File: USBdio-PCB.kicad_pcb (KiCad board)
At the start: 2 copper layers, 82.5 x 101.6 mm, 67 parts, among them IC1 ATMEGA328-P, P0 RELAY_(JSM1A-12V-4), P1 RELAY_(JSM1A-12V-4), P2 RELAY_(JSM1A-12V-4), P3 RELAY_(JSM1A-12V-4), P4 RELAY_(JSM1A-12V-4), P5 RELAY_(JSM1A-12V-4), P6 RELAY_(JSM1A-12V-4), P7 RELAY_(JSM1A-12V-4), P8 CONN_01X03, Q1 Q_NPN_BEC, Q10 Q_NPN, Q11 Q_NPN, Q12 Q_NPN, Q13 Q_NPN, Q14 Q_NPN, Q15 Q_NPN, Q16 Q_NPN, Q17 Q_NPN, Q2 Q_NPN_BEC, Q3 Q_NPN_BEC, Q4 Q_NPN_BEC, Q5 Q_NPN_BEC, Q6 Q_NPN_BEC, Q7 Q_NPN_BEC, Q8 Q_NPN_BEC, Q9 Q_NPN_BEC, U1 NCV7805BDTRKG, X1 CRYSTAL_SMD

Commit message: almost finish with traces.
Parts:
- moved P8 82.8 mm to (117.0, 63.6), turned to 90 degrees
- moved D4 39.4 mm to (158.6, 114.7), turned to 180 degrees
- moved D3 39.4 mm to (174.5, 114.7), turned to 180 degrees
- moved R22 39.1 mm to (164.1, 118.8)
- moved P4 39.1 mm to (148.4, 112.0)
- moved Q13 39.0 mm to (160.1, 119.2)
- moved P5 39.0 mm to (164.3, 112.0)
- moved Q12 39.0 mm to (176.0, 119.2)
- moved R21 38.2 mm to (179.1, 118.7)
- moved R23 32.3 mm to (147.8, 118.5)
- moved P3 32.0 mm to (132.4, 112.0)
- moved Q14 32.0 mm to (144.1, 119.3)
- moved D5 31.5 mm to (142.6, 114.8), turned to 180 degrees
- moved R24 27.6 mm to (148.1, 96.3)
- moved P2 27.5 mm to (132.4, 89.6)
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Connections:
- CONN_1 pad A2: GND -> Net-(CONN_1-PadA2)
- CONN_1 pad A3: GND -> Net-(CONN_1-PadA2)
- CONN_1 pad B1: Net-(CONN_1-PadA1) -> RLY4
- CONN_1 pad B10: RLY5 -> Net-(CONN_1-PadA1)
- CONN_1 pad B11: RLY6 -> Net-(CONN_1-PadA2)
- CONN_1 pad B12: RLY7 -> Net-(CONN_1-PadA2)
- CONN_1 pad B2: Net-(CONN_1-PadA1) -> RLY5
- CONN_1 pad B3: GND -> RLY6
- CONN_1 pad B4: GND -> RLY7
- CONN_1 pad B9: RLY4 -> Net-(CONN_1-PadA1)
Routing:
- net Net-(D1-Pad1): track 0.00 -> 333.6 mm, vias 0 -> 4
- net Net-(CONN_1-PadA1): track 0.00 -> 243.4 mm, vias 0 -> 2
- net +5V: track 0.00 -> 185.1 mm
- net Net-(CONN_1-PadB6): track 0.00 -> 166.0 mm
- net Net-(CONN_1-PadA5): track 0.00 -> 157.6 mm
- net Net-(CONN_1-PadB5): track 0.00 -> 155.2 mm, vias 0 -> 2
- net Net-(CONN_1-PadA6): track 0.00 -> 139.8 mm
- net Net-(CONN_1-PadB7): track 0.00 -> 132.1 mm
- net Net-(CONN_1-PadA7): track 0.00 -> 123.5 mm
- net Net-(CONN_1-PadB8): track 0.00 -> 117.5 mm
- net Net-(CONN_1-PadA8): track 0.00 -> 115.2 mm
- net Net-(CONN_1-PadA4): track 0.00 -> 96.0 mm, vias 0 -> 2
- net Net-(IC1-Pad15): track 0.00 -> 94.7 mm, vias 0 -> 2
- net Net-(IC1-Pad16): track 0.00 -> 82.5 mm, vias 0 -> 2
- net Net-(IC1-Pad17): track 0.00 -> 78.4 mm, vias 0 -> 2
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- added copper zone on B.Cu, net GND

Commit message: finished traces
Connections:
- CONN_1 pad A1: Net-(CONN_1-PadA1) -> GND
- CONN_1 pad A10: RLY1 -> RLY3
- CONN_1 pad A11: RLY2 -> Net-(CONN_1-PadA11)
- CONN_1 pad A12: RLY3 -> Net-(CONN_1-PadA12)
- CONN_1 pad A2: Net-(CONN_1-PadA2) -> GND
- CONN_1 pad A3: Net-(CONN_1-PadA2) -> Net-(CONN_1-PadA3)
- CONN_1 pad A7: Net-(CONN_1-PadA7) -> RLY0
- CONN_1 pad A8: Net-(CONN_1-PadA8) -> RLY1
- CONN_1 pad A9: RLY0 -> RLY2
- CONN_1 pad B1: RLY4 -> Net-(CONN_1-PadA12)
- CONN_1 pad B10: Net-(CONN_1-PadA1) -> Net-(CONN_1-PadB10)
- CONN_1 pad B11: Net-(CONN_1-PadA2) -> GND
- CONN_1 pad B12: Net-(CONN_1-PadA2) -> GND
- CONN_1 pad B2: RLY5 -> Net-(CONN_1-PadA12)
- CONN_1 pad B3: RLY6 -> RLY4
- CONN_1 pad B4: RLY7 -> RLY5
- CONN_1 pad B5: Net-(CONN_1-PadB5) -> RLY6
- CONN_1 pad B6: Net-(CONN_1-PadB6) -> RLY7
- CONN_1 pad B9: Net-(CONN_1-PadA1) -> Net-(CONN_1-PadB9)
- D9 pad 2: Net-(CONN_1-PadA1) -> Net-(CONN_1-PadA12)
- P0 pad 1: Net-(CONN_1-PadA1) -> Net-(CONN_1-PadA12)
- P1 pad 1: Net-(CONN_1-PadA1) -> Net-(CONN_1-PadA12)
- P2 pad 1: Net-(CONN_1-PadA1) -> Net-(CONN_1-PadA12)
- P3 pad 1: Net-(CONN_1-PadA1) -> Net-(CONN_1-PadA12)
- P4 pad 1: Net-(CONN_1-PadA1) -> Net-(CONN_1-PadA12)
- P5 pad 1: Net-(CONN_1-PadA1) -> Net-(CONN_1-PadA12)
- P6 pad 1: Net-(CONN_1-PadA1) -> Net-(CONN_1-PadA12)
- P7 pad 1: Net-(CONN_1-PadA1) -> Net-(CONN_1-PadA12)
- R10 pad 2: Net-(CONN_1-PadA8) -> Net-(CONN_1-PadA6)
- R12 pad 2: Net-(CONN_1-PadB5) -> Net-(CONN_1-PadB7)
- R14 pad 2: Net-(CONN_1-PadB6) -> Net-(CONN_1-PadB8)
- R16 pad 2: Net-(CONN_1-PadB7) -> Net-(CONN_1-PadB9)
- R18 pad 2: Net-(CONN_1-PadB8) -> Net-(CONN_1-PadB10)
- R2 pad 2: Net-(CONN_1-PadA4) -> Net-(CONN_1-PadA11)
- R4 pad 2: Net-(CONN_1-PadA5) -> Net-(CONN_1-PadA3)
- R6 pad 2: Net-(CONN_1-PadA6) -> Net-(CONN_1-PadA4)
- R8 pad 2: Net-(CONN_1-PadA7) -> Net-(CONN_1-PadA5)
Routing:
- net Net-(CONN_1-PadA1): track 243.4 -> 0.00 mm, vias 2 -> 0
- net Net-(CONN_1-PadA12): track 0.00 -> 223.5 mm, vias 0 -> 2
- net Net-(CONN_1-PadB6): track 166.0 -> 0.00 mm
- net Net-(CONN_1-PadB5): track 155.2 -> 0.00 mm, vias 2 -> 0
- net Net-(CONN_1-PadA3): track 0.00 -> 139.9 mm, vias 0 -> 1
- net Net-(CONN_1-PadA7): track 123.5 -> 0.00 mm
- net Net-(CONN_1-PadB10): track 0.00 -> 115.9 mm, vias 0 -> 1
- net Net-(CONN_1-PadA8): track 115.2 -> 0.00 mm
- net Net-(CONN_1-PadB9): track 0.00 -> 111.0 mm, vias 0 -> 1
- net Net-(CONN_1-PadA11): track 0.00 -> 80.3 mm, vias 0 -> 1
- net Net-(CONN_1-PadB8): track 117.5 -> 172.3 mm, vias 0 -> 1
- net Net-(CONN_1-PadA5): track 157.6 -> 121.4 mm, vias 0 -> 1
- net Net-(CONN_1-PadA4): track 96.0 -> 128.0 mm, vias 2 -> 1
- net Net-(CONN_1-PadA6): track 139.8 -> 111.8 mm, vias 0 -> 1
- net Net-(CONN_1-PadB7): track 132.1 -> 155.2 mm, vias 0 -> 1
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
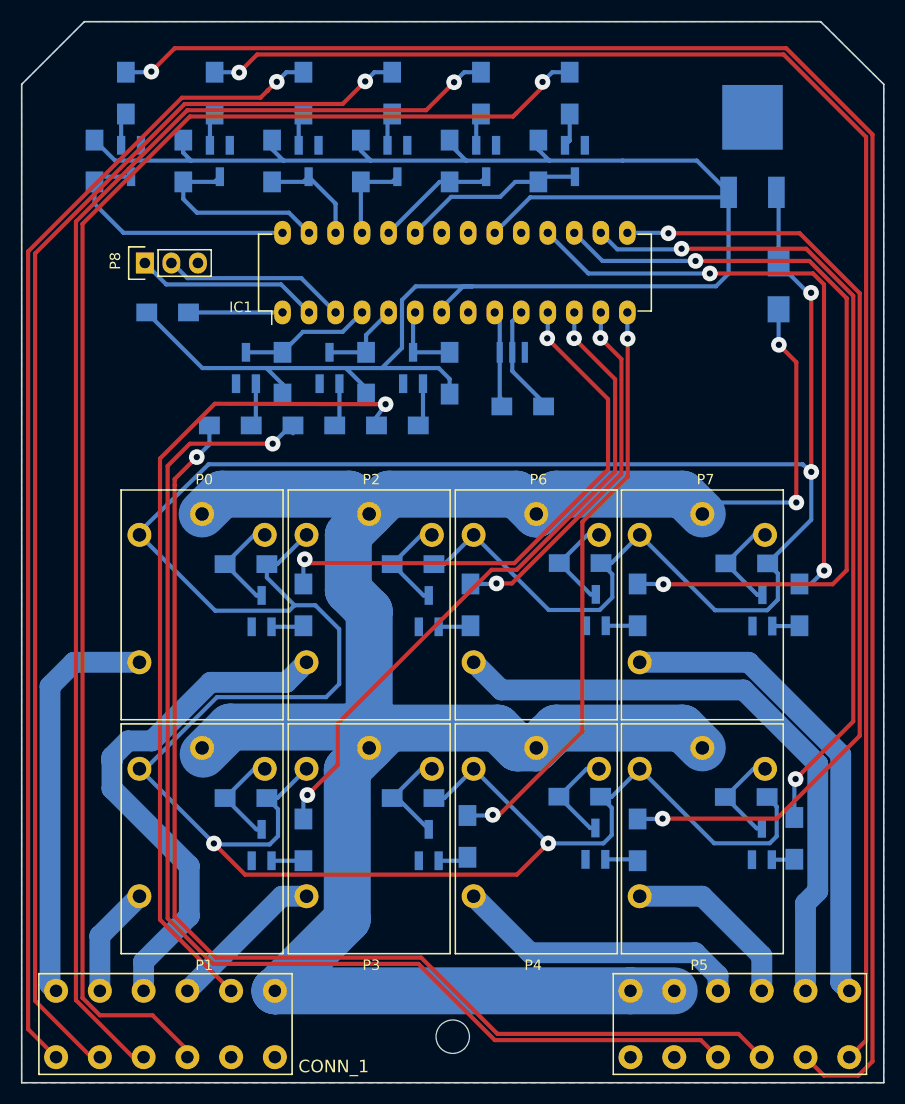
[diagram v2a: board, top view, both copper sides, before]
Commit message: Reduced to 6 in 6 out, and added COM lines to connector.
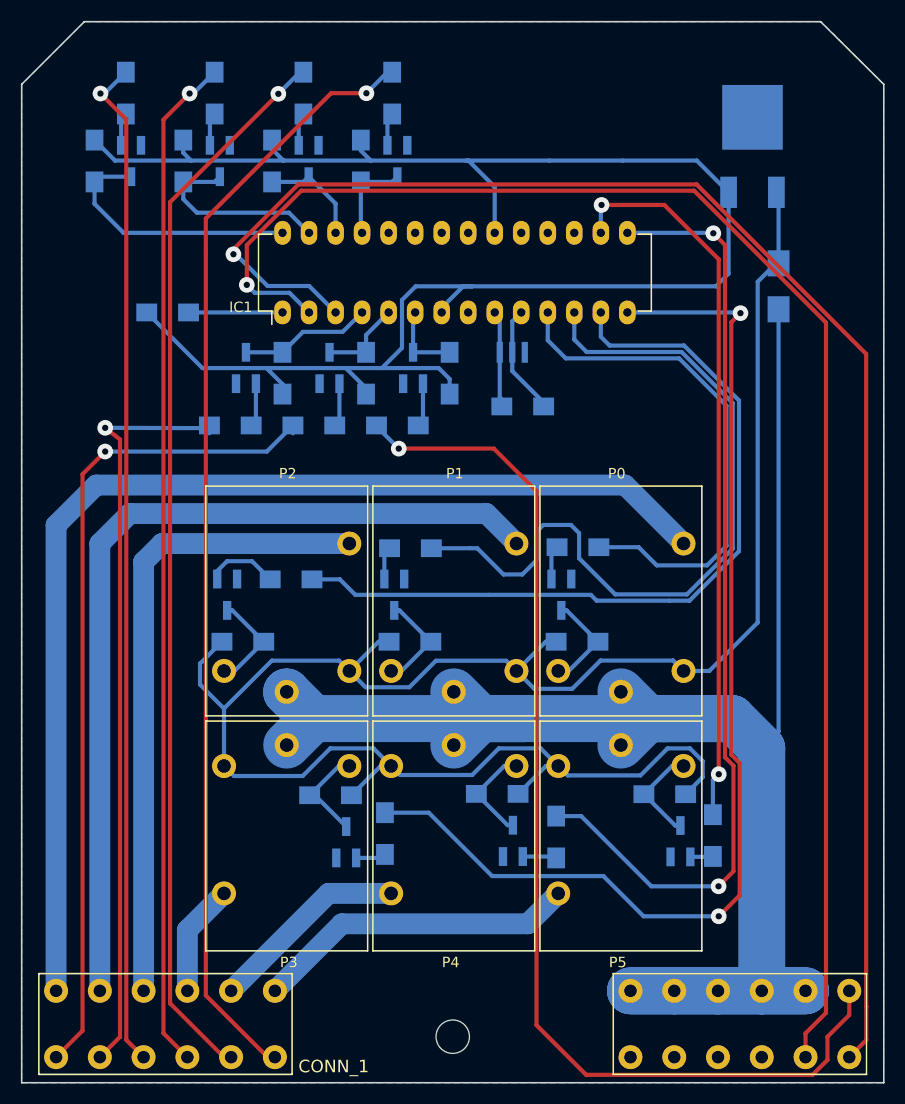
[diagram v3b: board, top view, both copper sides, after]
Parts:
- removed D1, D2: D, Resistors_SMD:R_1206_HandSoldering
- removed P6, P7: RELAY_(JSM1A-12V-4), USBdio-PCB:RELAY_(JSM1A-12V-4)
- removed P8: CONN_01X03, Pin_Headers:Pin_Header_Straight_1x03
- removed Q10, Q11: Q_NPN, TO_SOT_Packages_SMD:SOT-23_Handsoldering
- removed Q2, Q3: Q_NPN_BEC, TO_SOT_Packages_SMD:SOT-23_Handsoldering
- removed R19, R20: 680, Resistors_SMD:R_1206_HandSoldering
- removed R3, R4, R5, R6: 10k, Resistors_SMD:R_1206_HandSoldering
- moved P0 53.7 mm to (168.5, 102.7), turned to 270 degrees
- moved P1 37.3 mm to (152.5, 102.7), turned to 270 degrees
- moved D8 32.6 mm to (158.3, 99.9), turned to 0 degrees
- moved R25 29.7 mm to (142.4, 90.9), turned to 0 degrees
- moved Q17 28.7 mm to (156.8, 95.4), turned to 0 degrees
- moved Q16 27.1 mm to (140.8, 95.4), turned to 0 degrees
- moved R26 26.9 mm to (158.4, 90.8), turned to 0 degrees
- moved D7 21.7 mm to (142.3, 99.9), turned to 0 degrees
- moved Q15 19.4 mm to (124.8, 95.4), turned to 0 degrees
- moved D6 17.9 mm to (126.3, 99.9), turned to 0 degrees
- moved R24 17.4 mm to (131.0, 93.9), turned to 0 degrees
- moved P2 13.7 mm to (136.5, 102.7), turned to 270 degrees
- moved D4 7.90 mm to (150.7, 114.4)
- moved D5 7.90 mm to (134.7, 114.6)
- moved P3 7.90 mm to (124.5, 111.8)
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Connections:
- CONN_1 pad A1: GND -> Net-(CONN_1-PadA1)
- CONN_1 pad A11: Net-(CONN_1-PadA11) -> RLY4
- CONN_1 pad A12: Net-(CONN_1-PadA12) -> RLY5
- CONN_1 pad A2: GND -> Net-(CONN_1-PadA2)
- CONN_1 pad B1: Net-(CONN_1-PadA12) -> Net-(CONN_1-PadB1)
- CONN_1 pad B10: Net-(CONN_1-PadB10) -> GND
- CONN_1 pad B2: Net-(CONN_1-PadA12) -> Net-(CONN_1-PadB1)
- CONN_1 pad B3: RLY4 -> Net-(CONN_1-PadB1)
- CONN_1 pad B4: RLY5 -> Net-(CONN_1-PadB1)
- CONN_1 pad B5: RLY6 -> Net-(CONN_1-PadB1)
- CONN_1 pad B6: RLY7 -> Net-(CONN_1-PadB6)
- CONN_1 pad B7: Net-(CONN_1-PadB7) -> TXD
- CONN_1 pad B8: Net-(CONN_1-PadB8) -> RXD
- CONN_1 pad B9: Net-(CONN_1-PadB9) -> GND
- D9 pad 2: Net-(CONN_1-PadA12) -> Net-(CONN_1-PadB1)
- IC1 pad 2: Net-(IC1-Pad2) -> RXD
- IC1 pad 3: Net-(IC1-Pad3) -> TXD
- P0 pad 1: Net-(CONN_1-PadA12) -> Net-(CONN_1-PadB1)
- P1 pad 1: Net-(CONN_1-PadA12) -> Net-(CONN_1-PadB1)
- P2 pad 1: Net-(CONN_1-PadA12) -> Net-(CONN_1-PadB1)
- P3 pad 1: Net-(CONN_1-PadA12) -> Net-(CONN_1-PadB1)
- P4 pad 1: Net-(CONN_1-PadA12) -> Net-(CONN_1-PadB1)
- P5 pad 1: Net-(CONN_1-PadA12) -> Net-(CONN_1-PadB1)
- R10 pad 2: Net-(CONN_1-PadA6) -> Net-(CONN_1-PadA2)
- R12 pad 2: Net-(CONN_1-PadB7) -> Net-(CONN_1-PadA3)
- R14 pad 2: Net-(CONN_1-PadB8) -> Net-(CONN_1-PadA4)
- R16 pad 2: Net-(CONN_1-PadB9) -> Net-(CONN_1-PadA5)
- R18 pad 2: Net-(CONN_1-PadB10) -> Net-(CONN_1-PadA6)
- R2 pad 2: Net-(CONN_1-PadA11) -> Net-(CONN_1-PadB6)
- R8 pad 2: Net-(CONN_1-PadA5) -> Net-(CONN_1-PadA1)
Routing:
- net Net-(CONN_1-PadA12): track 223.5 -> 0.00 mm, vias 2 -> 0
- net Net-(CONN_1-PadB1): track 0.00 -> 189.6 mm
- net Net-(CONN_1-PadB8): track 172.3 -> 0.00 mm, vias 1 -> 0
- net Net-(CONN_1-PadB7): track 155.2 -> 0.00 mm, vias 1 -> 0
- net TXD: track 0.00 -> 150.5 mm, vias 0 -> 1
- net RXD: track 0.00 -> 144.9 mm, vias 0 -> 1
- net Net-(D3-Pad1): track 331.2 -> 193.0 mm, vias 4 -> 0
- net Net-(CONN_1-PadB10): track 115.9 -> 0.00 mm, vias 1 -> 0
- net Net-(CONN_1-PadB9): track 111.0 -> 0.00 mm, vias 1 -> 0
- net Net-(CONN_1-PadA1): track 0.00 -> 107.6 mm, vias 0 -> 1
- net Net-(CONN_1-PadB6): track 0.00 -> 107.0 mm, vias 0 -> 1
- net Net-(CONN_1-PadA2): track 0.00 -> 102.6 mm, vias 0 -> 1
- net Net-(CONN_1-PadA11): track 80.3 -> 0.00 mm, vias 1 -> 0
- net Net-(IC1-Pad17): track 75.3 -> 0.00 mm, vias 2 -> 0
- net RLY1: track 10.6 -> 85.1 mm
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
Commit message: -added CH340G and a self-resetting fuse -corrected errors from v1.1
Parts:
- added C1: 0.1uF, USBdio-PCB:R_1206_HandSoldering_(narrow), B.Cu at (157.4, 63.9)
- added C2: 0.1uF, USBdio-PCB:R_1206_HandSoldering_(narrow), B.Cu at (145.3, 53.9)
- added F1: Polyfuse, Resistors_SMD:R_1812_HandSoldering, B.Cu at (178.2, 68.3)
- added IC2: CH340G, USBdio-PCB:CH340G, B.Cu at (157.1, 48.6)
- added X2: Crystal_GND2, USBdio-PCB:RESONATOR_(CSTCE16M0V53C-R0), B.Cu at (165.5, 48.7)
- D3, D4, D5, D6, D7, D8, R1, R10, R11, R12, R13, R14, R15, R16, R17, R18, R2, R21, R22, R23, R24, R25, R26, R27, R28, R7, R8, R9: footprint Resistors_SMD:R_1206_HandSoldering -> USBdio-PCB:R_1206_HandSoldering_(narrow)
- X1: value CRYSTAL_SMD -> Crystal_GND2
- moved D9 14.5 mm to (178.0, 80.3)
- moved R1 0.50 mm to (146.1, 73.6)
- moved R17 0.50 mm to (138.1, 73.6)
- moved R15 0.44 mm to (130.1, 73.7)
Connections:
- CONN_1 pad B7: TXD -> D+
- CONN_1 pad B8: RXD -> D-
- D9 pad 1: Net-(D3-Pad1) -> Net-(D9-Pad1)
- X1 pad 2: Net-(IC1-Pad10) -> GND
- X1 pad 3: GND -> Net-(IC1-Pad10)
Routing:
- net D+: track 0.00 -> 127.1 mm
- net D-: track 0.00 -> 122.6 mm
- net TXD: track 150.5 -> 38.2 mm, vias 1 -> 2
- net RXD: track 144.9 -> 43.8 mm, vias 1 -> 2
- net Net-(C2-Pad1): track 9.00 -> 32.7 mm
- net Net-(CONN_1-PadB1): track 189.6 -> 173.7 mm
- net Net-(C2-Pad2): track 0.00 -> 13.2 mm
- net GND: track 0.00 -> 9.92 mm
- net Net-(IC2-Pad8): track 0.00 -> 7.17 mm
- net Net-(D9-Pad1): track 0.00 -> 6.51 mm
- net Net-(IC2-Pad7): track 0.00 -> 6.44 mm
- net +5V: track 169.8 -> 174.5 mm
- net Net-(D3-Pad1): track 193.0 -> 192.2 mm
- added copper zone on F.Cu, net GND
